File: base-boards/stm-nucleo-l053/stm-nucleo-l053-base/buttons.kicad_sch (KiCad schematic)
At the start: 16 parts, among them SW1 SW_SPST

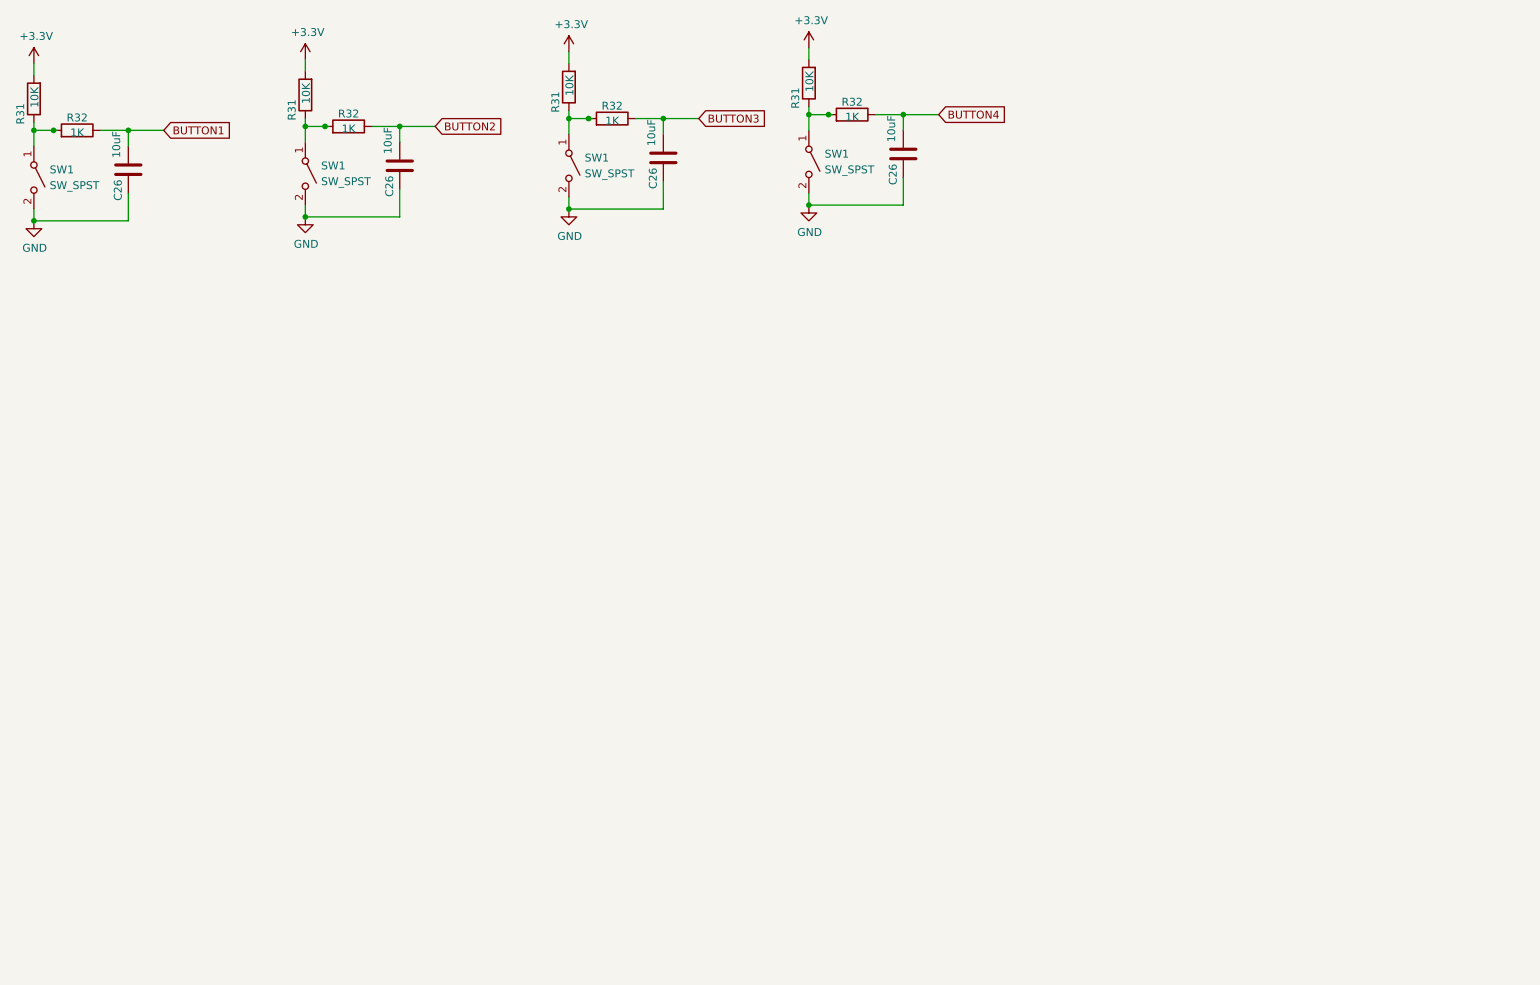
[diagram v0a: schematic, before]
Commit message: Added Arduino Nano breakout
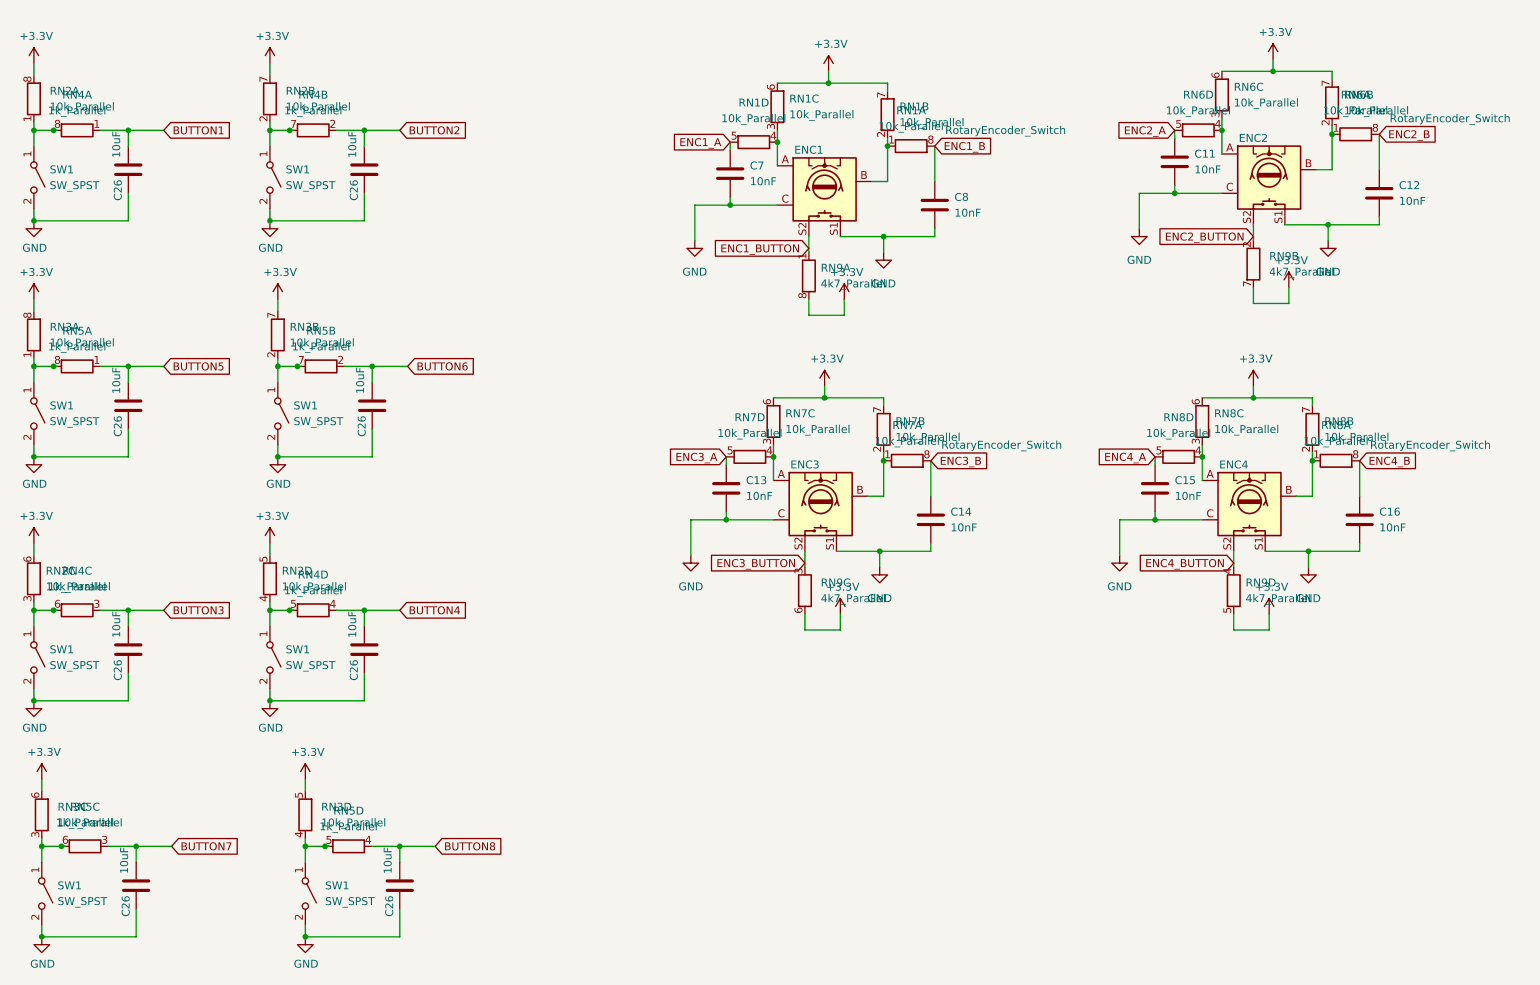
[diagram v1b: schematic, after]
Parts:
- removed R31 (x4): 10K, Resistor_SMD:R_0603_1608Metric_Pad0.98x0.95mm_HandSolder, symbol KPM-Passives:R-0603-10K-0.1W-1%
- removed R32 (x4): 1K, Resistor_SMD:R_0603_1608Metric_Pad0.98x0.95mm_HandSolder, symbol KPM-Passives:R-0603-1K-0.1W-1%
- added C11, C12, C13, C14, C15, C16, C7, C8: 10nF, Capacitor_SMD:C_0603_1608Metric_Pad1.08x0.95mm_HandSolder, symbol Device:C
- added C26 (x4): 10uF, Capacitor_SMD:C_0603_1608Metric_Pad1.08x0.95mm_HandSolder, symbol KPM-Passives:C-0603-10uF-35V
- added ENC1, ENC2, ENC3, ENC4: RotaryEncoder_Switch, Rotary_Encoder:RotaryEncoder_Alps_EC12E-Switch_Vertical_H20mm, symbol KPM-Interface:RotaryEncoder_Switch
- added RN1, RN2, RN3, RN6, RN7, RN8: 10k_Parallel, Resistor_SMD:R_Array_Concave_4x0603, symbol Device:R_Pack04_Split
- added RN4, RN5: 1k_Parallel, Resistor_SMD:R_Array_Concave_4x0603, symbol Device:R_Pack04_Split
- added RN9: 4k7_Parallel, Resistor_SMD:R_Array_Concave_4x0603, symbol Device:R_Pack04_Split
- added SW1 (x4): SW_SPST, Button_Switch_SMD:SW_SPST_Omron_B3FS-101xP, symbol Switch:SW_SPST
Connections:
- net +3.3V: now also RN1.6 (R3.2), RN1.7 (R2.2), RN2.5 (R4.2), RN2.6 (R3.2), RN2.7 (R2.2), RN2.8 (R1.2), RN3.5 (R4.2), RN3.6 (R3.2), RN3.7 (R2.2), RN3.8 (R1.2), RN6.6 (R3.2), RN6.7 (R2.2), RN7.6 (R3.2), RN7.7 (R2.2), RN8.6 (R3.2), RN8.7 (R2.2), RN9.5 (R4.2), RN9.6 (R3.2), RN9.7 (R2.2), RN9.8 (R1.2)
- net BUTTON1: now also RN4.1 (R1.1)
- net BUTTON2: now also RN4.2 (R2.1)
- net BUTTON3: now also RN4.3 (R3.1)
- net BUTTON4: now also RN4.4 (R4.1)
- net GND: now also C11.2, C12.2, C13.2, C14.2, C15.2, C16.2, C26.1, C26.1, C26.1, C26.1, C7.2, C8.2, ENC1.C, ENC1.S1, ENC2.C, ENC2.S1, ENC3.C, ENC3.S1, ENC4.C, ENC4.S1, SW1.2 (B), SW1.2 (B), SW1.2 (B), SW1.2 (B)
- net at SW1.1 (A): now also RN2.1 (R1.1), RN4.8 (R1.2)
- net at SW1.1 (A): now also RN2.3 (R3.1), RN4.6 (R3.2)
- net at SW1.1 (A): now also RN2.4 (R4.1), RN4.5 (R4.2)
- net at SW1.1 (A): now also RN2.2 (R2.1), RN4.7 (R2.2)
- new net: ENC4.B, RN8.1 (R1.1), RN8.2 (R2.1)
- new net: ENC3.B, RN7.1 (R1.1), RN7.2 (R2.1)
- new net: RN3.3 (R3.1), RN5.6 (R3.2), SW1.1 (A)
- new net: ENC3.A, RN7.3 (R3.1), RN7.4 (R4.1)
- new net: RN3.2 (R2.1), RN5.7 (R2.2), SW1.1 (A)
- new net: ENC4.A, RN8.3 (R3.1), RN8.4 (R4.1)
- new net: ENC1.A, RN1.3 (R3.1), RN1.4 (R4.1)
- new net: ENC1.B, RN1.1 (R1.1), RN1.2 (R2.1)
- new net: RN3.1 (R1.1), RN5.8 (R1.2), SW1.1 (A)
- new net: RN3.4 (R4.1), RN5.5 (R4.2), SW1.1 (A)
- new net: ENC2.A, RN6.3 (R3.1), RN6.4 (R4.1)
- new net: ENC2.B, RN6.1 (R1.1), RN6.2 (R2.1)
- new net BUTTON5: C26.2, RN5.1 (R1.1)
- new net BUTTON6: C26.2, RN5.2 (R2.1)
- new net BUTTON7: C26.2, RN5.3 (R3.1)
- new net BUTTON8: C26.2, RN5.4 (R4.1)
- new net ENC1_A: C7.1, RN1.5 (R4.2)
- new net ENC1_B: C8.1, RN1.8 (R1.2)
- new net ENC1_BUTTON: ENC1.S2, RN9.1 (R1.1)
- new net ENC2_A: C11.1, RN6.5 (R4.2)
- new net ENC2_B: C12.1, RN6.8 (R1.2)
- new net ENC2_BUTTON: ENC2.S2, RN9.2 (R2.1)
- new net ENC3_A: C13.1, RN7.5 (R4.2)
- new net ENC3_B: C14.1, RN7.8 (R1.2)
- new net ENC3_BUTTON: ENC3.S2, RN9.3 (R3.1)
- new net ENC4_A: C15.1, RN8.5 (R4.2)
- new net ENC4_B: C16.1, RN8.8 (R1.2)
- new net ENC4_BUTTON: ENC4.S2, RN9.4 (R4.1)
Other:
- moved on the sheet: C26, SW1
